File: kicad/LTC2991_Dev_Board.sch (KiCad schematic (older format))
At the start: 12 parts, among them P1 PIN_HEAD_1x8, P2 PIN_HEAD_1x8, P3 PIN_HEAD_2x3, P4 CONN_SENSE, Q1 MMBT3904, U1 LTC2991

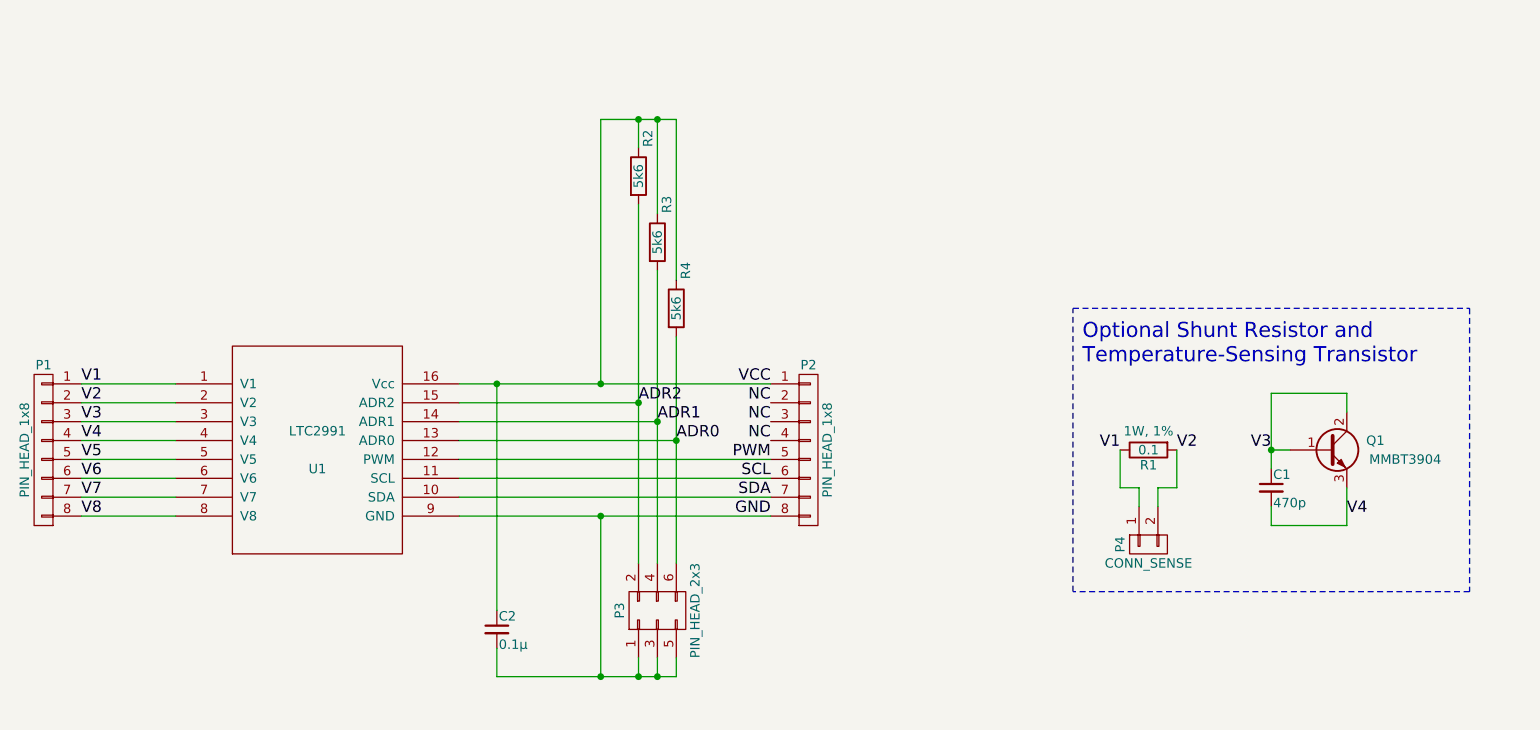
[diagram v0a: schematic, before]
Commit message: Cleaned up schematic for sake of readability.  No functional changes.
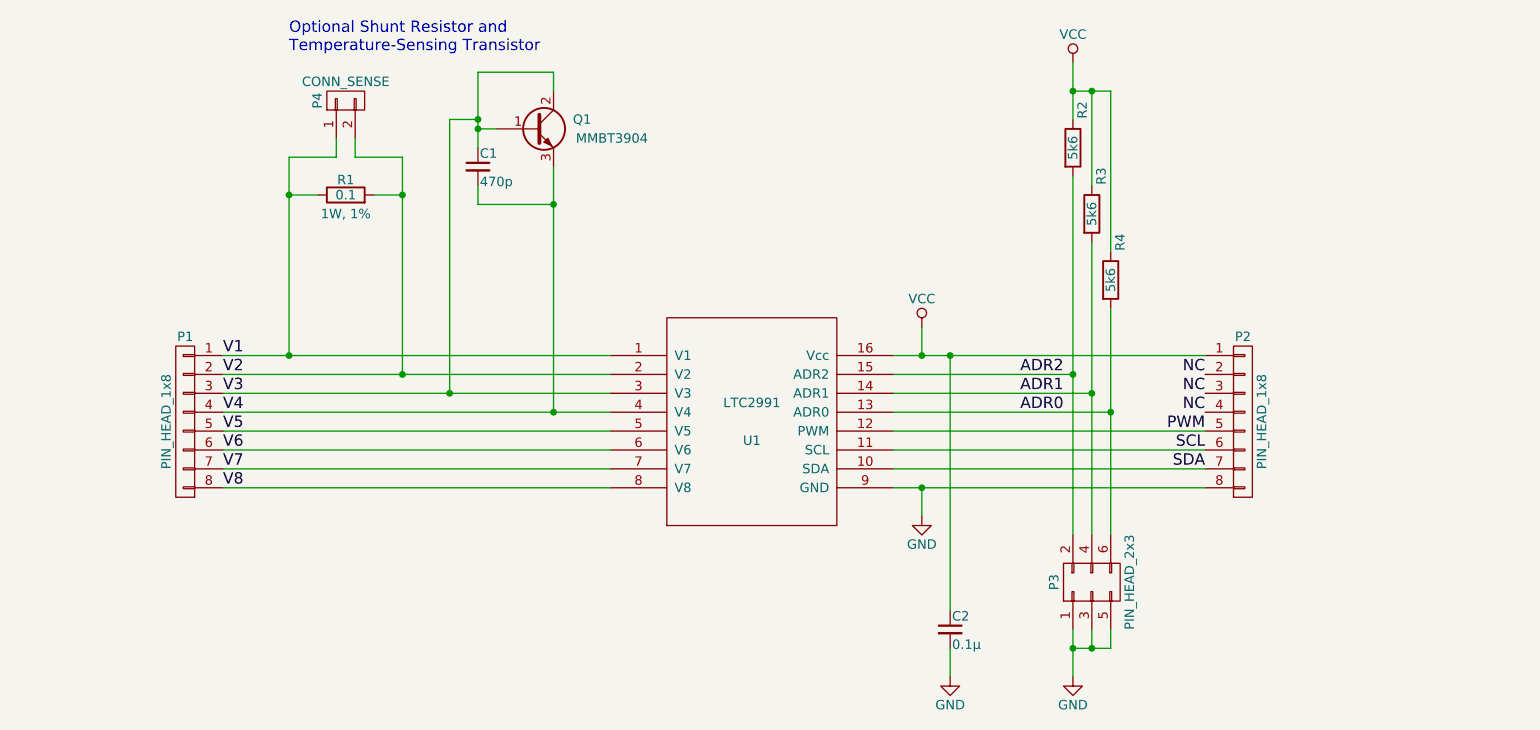
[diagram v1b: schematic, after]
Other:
- moved on the sheet: C1, C2, P1, P2, P3, P4, Q1, R1, R2, R3, R4, U1
